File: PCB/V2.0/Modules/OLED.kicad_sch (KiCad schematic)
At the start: 3 parts, among them J14 OLED_SOCKET, J16 I2C_Selector, J22 OLED_SOCKET_VIRTUAL

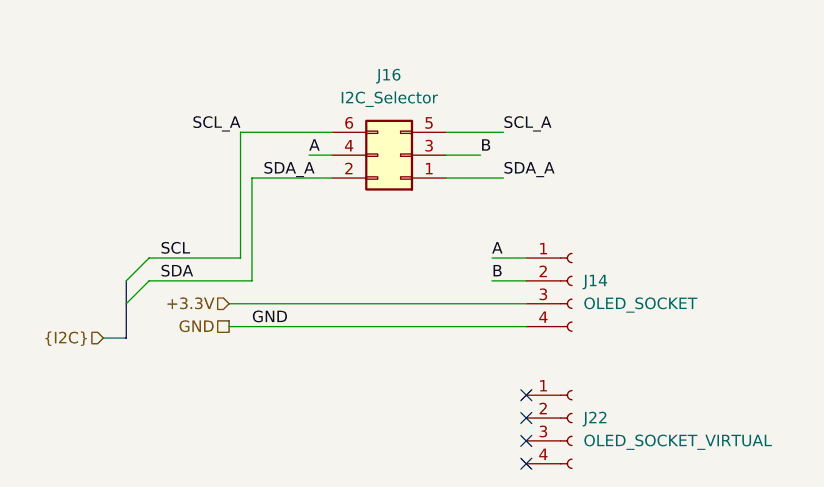
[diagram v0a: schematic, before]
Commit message: Update of BME and OLED
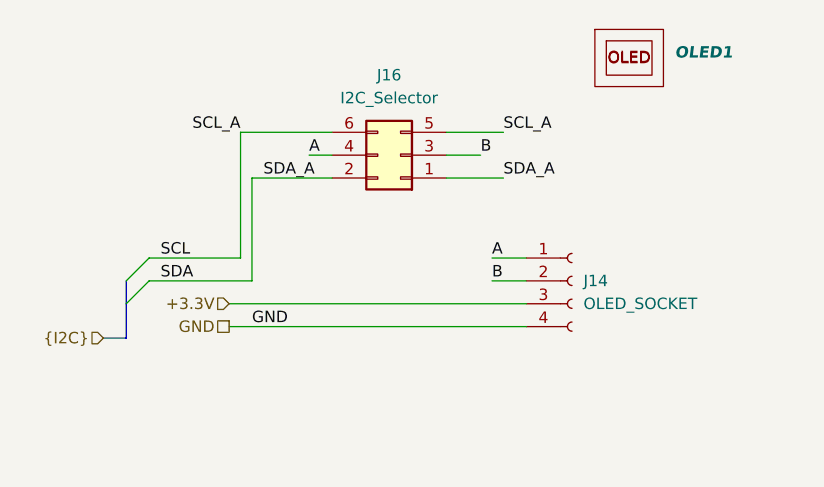
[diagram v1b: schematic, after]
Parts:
- removed J22: OLED_SOCKET_VIRTUAL, Connector_PinSocket_2.54mm:PinSocket_1x04_P2.54mm_Vertical, symbol Connector:Conn_01x04_Socket
- added OLED1: ~, CREPP_Screens:SSD1306_OLED_Display_VIRTUAL_128_64, symbol CREPP_Screens:OLED_SSD1306_0.96
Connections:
- no-connect marks 4 -> 0
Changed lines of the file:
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@@
 		(company "Designed by CREPP-NLG")
-	)
-	(no_connect
-		(at 119.38 81.28)
-	)
-	(no_connect
-		(at 119.38 76.2)
-	)
-	(no_connect
-		(at 119.38 78.74)
-	)
-	(no_connect
-		(at 119.38 83.82)
 	)
 	(bus_entry
@@
 	)
 	(symbol
-		(lib_id "Connector:Conn_01x04_Socket")
-		(at 124.46 78.74 0)
+		(lib_id "CREPP_Screens:OLED_SSD1306_0.96")
+		(at 130.81 39.37 0)
 		(unit 1)
 		(exclude_from_sim no)
@@
 		(dnp no)
 		(fields_autoplaced yes)
-		(property "Reference" "J22"
-			(at 125.73 78.7399 0)
-			(effects
-				(font
-					(size 1.27 1.27)
+		(property "Reference" "OLED1"
+			(at 135.89 38.1 0)
+			(effects
+				(font
+					(size 1.27 1.27)
+					(bold yes)
+					(italic yes)
+					(color 0 132 0 1)
 				)
 				(justify left)
 			)
 		)
-		(property "Value" "OLED_SOCKET_VIRTUAL"
-			(at 125.73 81.2799 0)
+		(property "Value" "~"
+			(at 135.89 40.005 0)
 			(effects
 				(font
@@
 			)
 		)
-		(property "Footprint" "Connector_PinSocket_2.54mm:PinSocket_1x04_P2.54mm_Vertical"
-			(at 124.46 78.74 0)
-			(effects
-				(font
-					(size 1.27 1.27)
-				)
-				(hide yes)
-			)
-		)
-		(property "Datasheet" "~"
-			(at 124.46 78.74 0)
-			(effects
-				(font
-					(size 1.27 1.27)
-				)
-				(hide yes)
-			)
-		)
-		(property "Description" "Generic connector, single row, 01x04, script generated"
-			(at 124.46 78.74 0)
-			(effects
-				(font
-					(size 1.27 1.27)
-				)
-				(hide yes)
-			)
-		)
-		(pin "4"
-		)
-		(pin "3"
-		)
-		(pin "2"
-		)
-		(pin "1"
+		(property "Footprint" "CREPP_Screens:SSD1306_OLED_Display_VIRTUAL_128_64"
+			(at 130.81 33.02 0)
+			(effects
+				(font
+					(size 1.27 1.27)
+				)
+				(hide yes)
+			)
+		)
+		(property "Datasheet" ""
+			(at 130.81 33.02 0)
+			(effects
+				(font
+					(size 1.27 1.27)
+				)
+				(hide yes)
+			)
+		)
+		(property "Description" ""
+			(at 130.81 33.02 0)
+			(effects
+				(font
+					(size 1.27 1.27)
+				)
+				(hide yes)
+			)
 		)
 		(instances
 			(project "CREPP.io"
 				(path "/8bcd0d00-b75f-4070-8d50-196a2022a31c/a3954905-38ea-4d92-9f94-5da1e2d350f3"
-					(reference "J22")
+					(reference "OLED1")
 					(unit 1)
 				)

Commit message: Update board
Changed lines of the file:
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@@
 	(label "A"
 		(at 115.57 60.96 0)
-		(fields_autoplaced yes)
 		(effects
 			(font
@@
 	(label "SDA"
 		(at 78.74 63.5 0)
-		(fields_autoplaced yes)
 		(effects
 			(font
@@
 	(label "A"
 		(at 95.25 49.53 0)
-		(fields_autoplaced yes)
 		(effects
 			(font
@@
 	(label "B"
 		(at 114.3 49.53 0)
-		(fields_autoplaced yes)
 		(effects
 			(font
@@
 	(label "SCL_A"
 		(at 87.63 46.99 180)
-		(fields_autoplaced yes)
 		(effects
 			(font
@@
 	(label "SCL_A"
 		(at 116.84 46.99 0)
-		(fields_autoplaced yes)
 		(effects
 			(font
@@
 	(label "SDA_A"
 		(at 90.17 52.07 0)
-		(fields_autoplaced yes)
 		(effects
 			(font
@@
 	(label "SDA_A"
 		(at 116.84 52.07 0)
-		(fields_autoplaced yes)
 		(effects
 			(font
@@
 	(label "B"
 		(at 115.57 63.5 0)
-		(fields_autoplaced yes)
 		(effects
 			(font
@@
 	(label "GND"
 		(at 88.9 68.58 0)
-		(fields_autoplaced yes)
 		(effects
 			(font
@@
 	(label "SCL"
 		(at 78.74 60.96 0)
-		(fields_autoplaced yes)
 		(effects
 			(font
@@
 		)
 	)
-	(hierarchical_label "{I2C}"
-		(shape input)
+	(hierarchical_label "{I2C0}"
+		(shape bidirectional)
 		(at 72.39 69.85 180)
-		(fields_autoplaced yes)
 		(effects
 			(font
@@
 		(shape passive)
 		(at 86.36 68.58 180)
-		(fields_autoplaced yes)
 		(effects
 			(font
@@
 		(shape input)
 		(at 86.36 66.04 180)
-		(fields_autoplaced yes)
 		(effects
 			(font

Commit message: Update
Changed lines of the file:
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@@
+	)
+	(symbol
+		(lib_id "CREPP_Screens:OLED_SSD1306_0.96")
+		(at 129.54 38.1 0)
+		(unit 1)
+		(exclude_from_sim no)
+		(in_bom yes)
+		(on_board yes)
+		(dnp no)
+		(fields_autoplaced yes)
+		(property "Reference" "OLED1"
+			(at 134.62 36.83 0)
+			(effects
+				(font
+					(size 1.27 1.27)
+					(bold yes)
+					(italic yes)
+					(color 0 132 0 1)
+				)
+				(justify left)
+			)
+		)
+		(property "Value" "~"
+			(at 134.62 38.735 0)
+			(effects
+				(font
+					(size 1.27 1.27)
+				)
+				(justify left)
+			)
+		)
+		(property "Footprint" "CREPP_Screens:SSD1306_OLED_Display_VIRTUAL_128_64"
+			(at 129.54 31.75 0)
+			(effects
+				(font
+					(size 1.27 1.27)
+				)
+				(hide yes)
+			)
+		)
+		(property "Datasheet" ""
+			(at 129.54 31.75 0)
+			(effects
+				(font
+					(size 1.27 1.27)
+				)
+				(hide yes)
+			)
+		)
+		(property "Description" ""
+			(at 129.54 31.75 0)
+			(effects
+				(font
+					(size 1.27 1.27)
+				)
+				(hide yes)
+			)
+		)
+		(instances
+			(project ""
+				(path "/8bcd0d00-b75f-4070-8d50-196a2022a31c/a3954905-38ea-4d92-9f94-5da1e2d350f3"
+					(reference "OLED1")
+					(unit 1)
+				)
+			)
+		)
 	)
 	(symbol
@@
 					(unit 1)
 				)
-			)
-		)
-	)
-	(symbol
-		(lib_id "CREPP_Screens:OLED_SSD1306_0.96")
-		(at 130.81 39.37 0)
-		(unit 1)
-		(exclude_from_sim no)
-		(in_bom yes)
-		(on_board yes)
-		(dnp no)
-		(fields_autoplaced yes)
-		(property "Reference" "OLED1"
-			(at 135.89 38.1 0)
-			(effects
-				(font
-					(size 1.27 1.27)
-					(bold yes)
-					(italic yes)
-					(color 0 132 0 1)
-				)
-				(justify left)
-			)
-		)
-		(property "Value" "~"
-			(at 135.89 40.005 0)
-			(effects
-				(font
-					(size 1.27 1.27)
-				)
-				(justify left)
-			)
-		)
-		(property "Footprint" "CREPP_Screens:SSD1306_OLED_Display_VIRTUAL_128_64"
-			(at 130.81 33.02 0)
-			(effects
-				(font
-					(size 1.27 1.27)
-				)
-				(hide yes)
-			)
-		)
-		(property "Datasheet" ""
-			(at 130.81 33.02 0)
-			(effects
-				(font
-					(size 1.27 1.27)
-				)
-				(hide yes)
-			)
-		)
-		(property "Description" ""
-			(at 130.81 33.02 0)
-			(effects
-				(font
-					(size 1.27 1.27)
-				)
-				(hide yes)
-			)
-		)
-		(instances
-			(project "CREPP.io"
-				(path "/8bcd0d00-b75f-4070-8d50-196a2022a31c/a3954905-38ea-4d92-9f94-5da1e2d350f3"
-					(reference "OLED1")
-					(unit 1)
-				)
